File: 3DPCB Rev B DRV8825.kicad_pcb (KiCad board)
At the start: 2 copper layers, 100 x 60 mm, 838 parts, among them IC1 DRV8825, IC2 DRV8825, IC3 DRV8825, IC4 DRV8825, IC5 DRV8825, J1 SOLDER_JUMPER_3P, J10 , J11 , J12 , J13 , J14 , J15 , J16 , J2 , J3 , J4 , J5 , J6 , J7 , J8 , J9 , K1 CONN_3, K2 CONN_3, K3 CONN_3, K4 CONN_3, K5 CONN_3, K6 CONN_3, K7 CONN_3, P1 CONN_8, P10 CONN_2, P11 CONN_3X2, P12 CONN_3X2, P13 CONN_4, P2 CONN_2, P3 CONN_2, P4 CONN_2, P5 CONN_4, P6 CONN_4, P7 CONN_4, P8 CONN_2, P9 CONN_4, U1 CONN_4_LERCHE, U10 MICRO-SD, U11 TC4427, U12 MCP4728, U13 CONN_4_LERCHE, U15 SPST_MOMENTARY, U16 CONN_4_LERCHE, U17 TC4427, U2 SPST_MOMENTARY, U20 TPS6213X, U21 CONN_4_LERCHE, U22 CONN_4_LERCHE, U23 MCP4728, U24 MOS_NFET, U25 CONN_4_LERCHE, U3 BSS84, U4 CONN_4_LERCHE, U5 MOS_NFET, U6 LPC1768_TQFP100, U7 MOS_NFET, U8 MOS_NFET, U9 CRYSTAL_SMALL

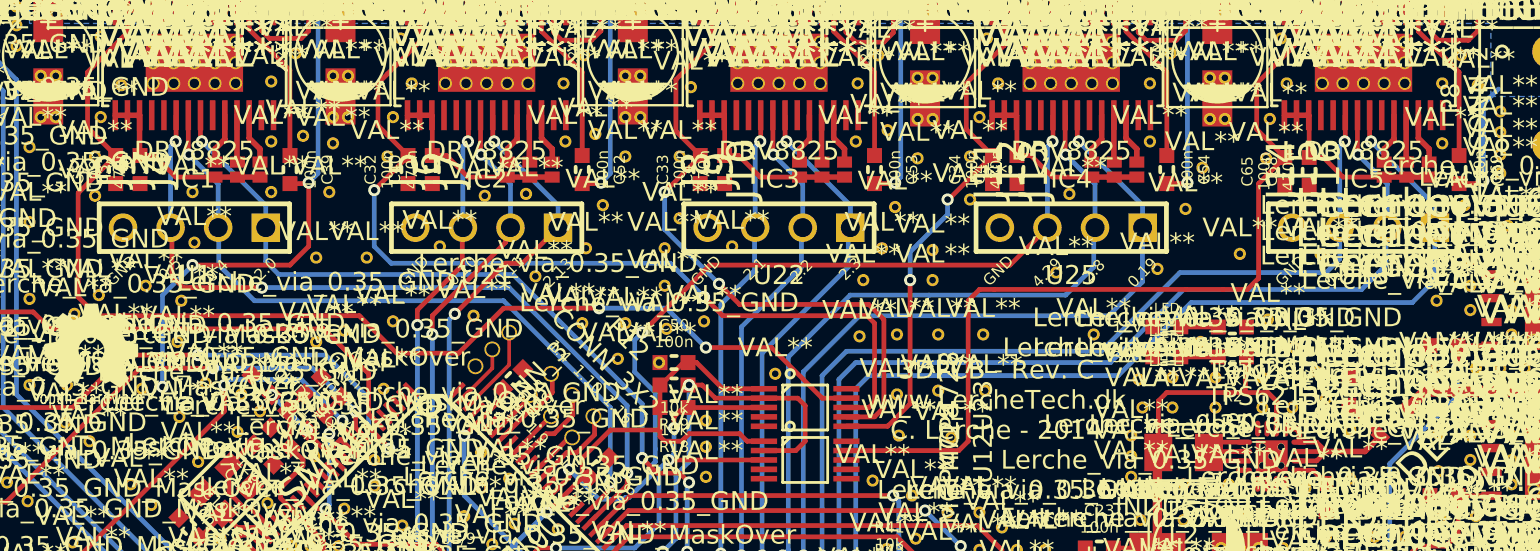
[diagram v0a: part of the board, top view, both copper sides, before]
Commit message: Added wiring for 3V3 for DRV8825 - NOT TESTED
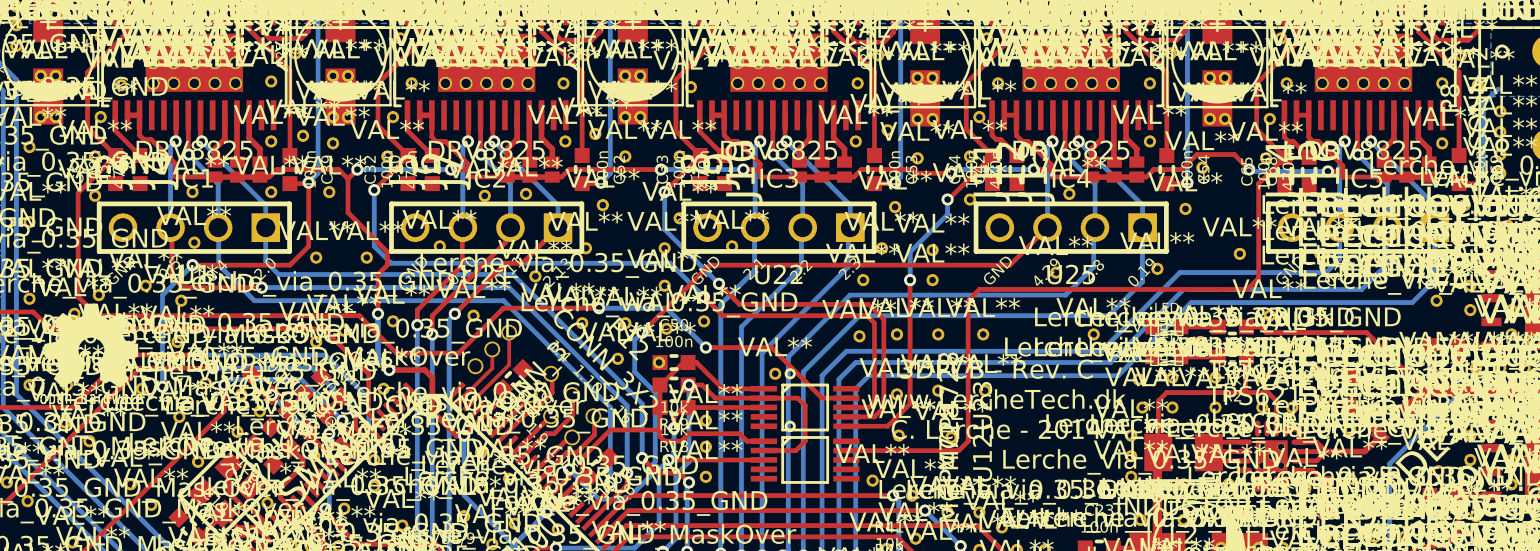
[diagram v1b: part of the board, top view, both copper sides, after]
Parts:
- moved ? 0.22 mm to (207.1, 159.8)
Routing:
- net +3.3V: track 290.1 -> 357.5 mm, vias 19 -> 29
- net +12V: track 155.1 -> 166.1 mm
- net N-0000059: track 1.40 -> 2.95 mm
- net N-0000037: track 1.40 -> 2.85 mm
- net N-0000033: track 1.40 -> 2.73 mm
- net N-0000053: track 1.40 -> 2.70 mm
- net N-00000190: track 1.44 -> 2.73 mm
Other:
- board text added: "PROVIDED AS IS 3DPCB is my design, scheamtic is almost all from Smoothieboard, but this board is designed to fit other PCBs like Printrboard and others. CODE-CHANGES NEEDED TO USE THIS BOARD: The DAC is not native to Smoothie, so I wrote my own code to use it. If you're using it and you need the code, write to me on Hackaday.io or on Lerche@lerchetech.dk Last but most important: Have fun!"
